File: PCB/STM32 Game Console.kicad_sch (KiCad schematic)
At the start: 5 parts, among them J1 CN7, J2 CN10

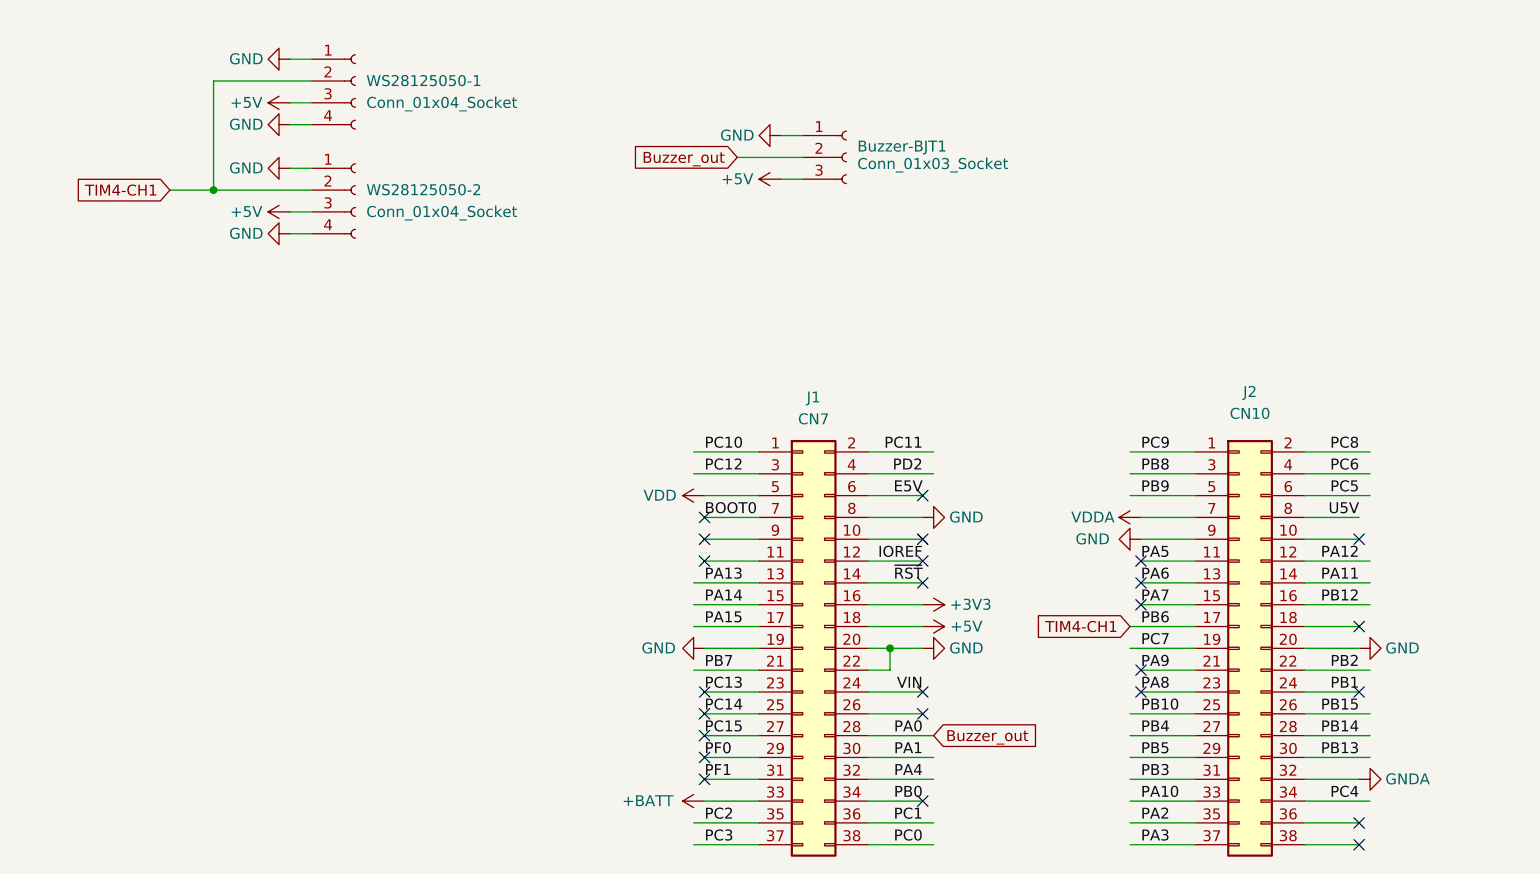
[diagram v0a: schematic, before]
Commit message: feat add: add SD_card schematic
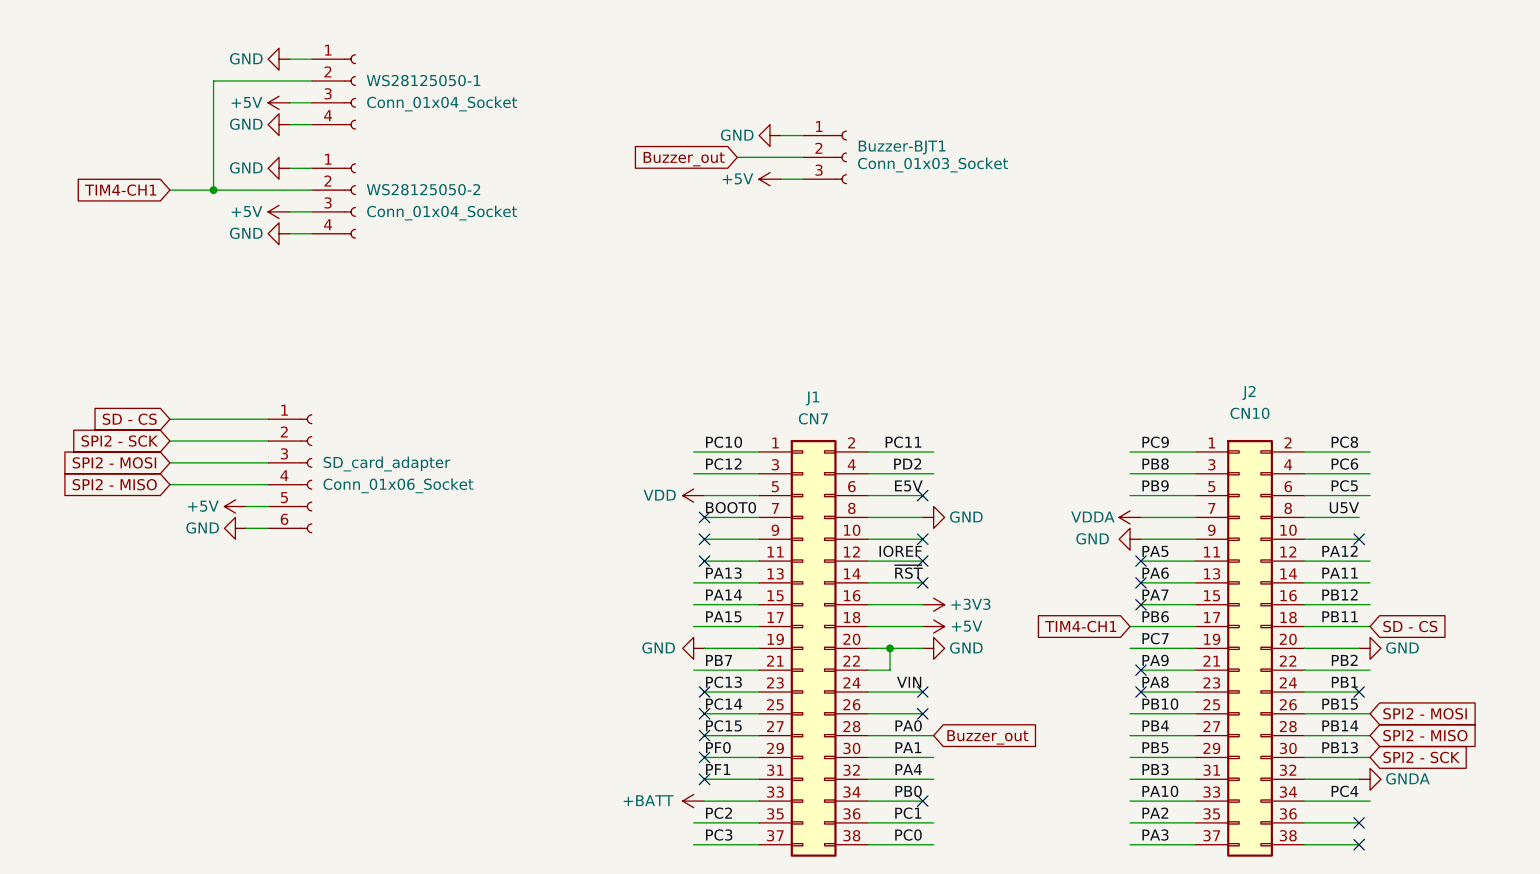
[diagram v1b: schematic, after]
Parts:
- added SD_card_adapter: Conn_01x06_Socket, symbol Connector:Conn_01x06_Socket
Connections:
- net +5V: now also SD_card_adapter.5 (Pin_5)
- net GND: now also SD_card_adapter.6 (Pin_6)
- net SD - CS: now reaches J2.18 (Pin_18)
- net SD - CS: now also SD_card_adapter.1 (Pin_1)
- net PB13 renamed SPI2 - SCK
- net SPI2 - SCK: now also SD_card_adapter.2 (Pin_2)
- net PB14 renamed SPI2 - MISO
- net SPI2 - MISO: now also SD_card_adapter.4 (Pin_4)
- net PB15 renamed SPI2 - MOSI
- net SPI2 - MOSI: now also SD_card_adapter.3 (Pin_3)
- no-connect marks 25 -> 24

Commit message: Change PCB design
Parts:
- removed Buzzer-BJT1: Conn_01x03_Socket, Connector_PinSocket_2.54mm:PinSocket_1x03_P2.54mm_Horizontal, symbol Connector:Conn_01x03_Socket
- added BZ1: Buzzer, symbol Device:Buzzer
- added Q1: Q_NPN_BCE, symbol Device:Q_NPN_BCE
- added R1: R, symbol Device:R
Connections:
- net +5V: now also BZ1.1 (+)
- net Buzzer_out: now also R1.1
- net GND: now also Q1.3 (E)
- new net: Q1.1 (B), R1.2
- new net: BZ1.2 (-), Q1.2 (C)
